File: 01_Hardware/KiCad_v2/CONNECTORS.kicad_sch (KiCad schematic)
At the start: 45 parts, among them J800 Conn_02x03_Odd_Even, J801 JST_B2B, J802 JST_B2B, J803 JST_B2B, J804 Conn_02x05_Odd_Even, J805 JST_B2B, J806 JST_B2B, J807 JST_B2B, J808 JST_B2B, SW800 SW_Push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

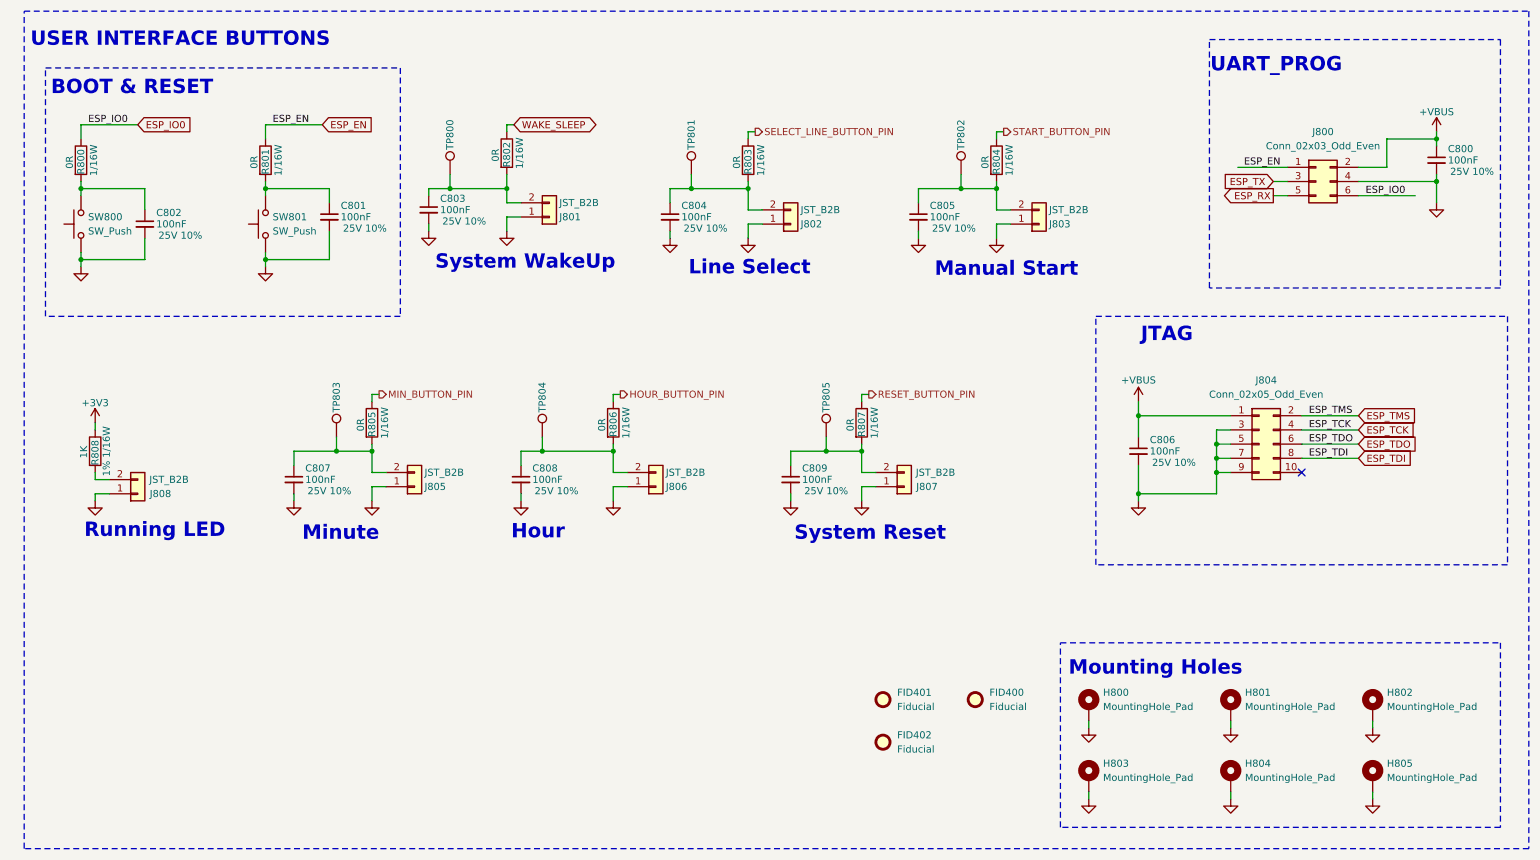
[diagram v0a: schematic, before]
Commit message: BOM done, except connectors/thermistor/button -> Will re-check BOM before sending to manufacturing
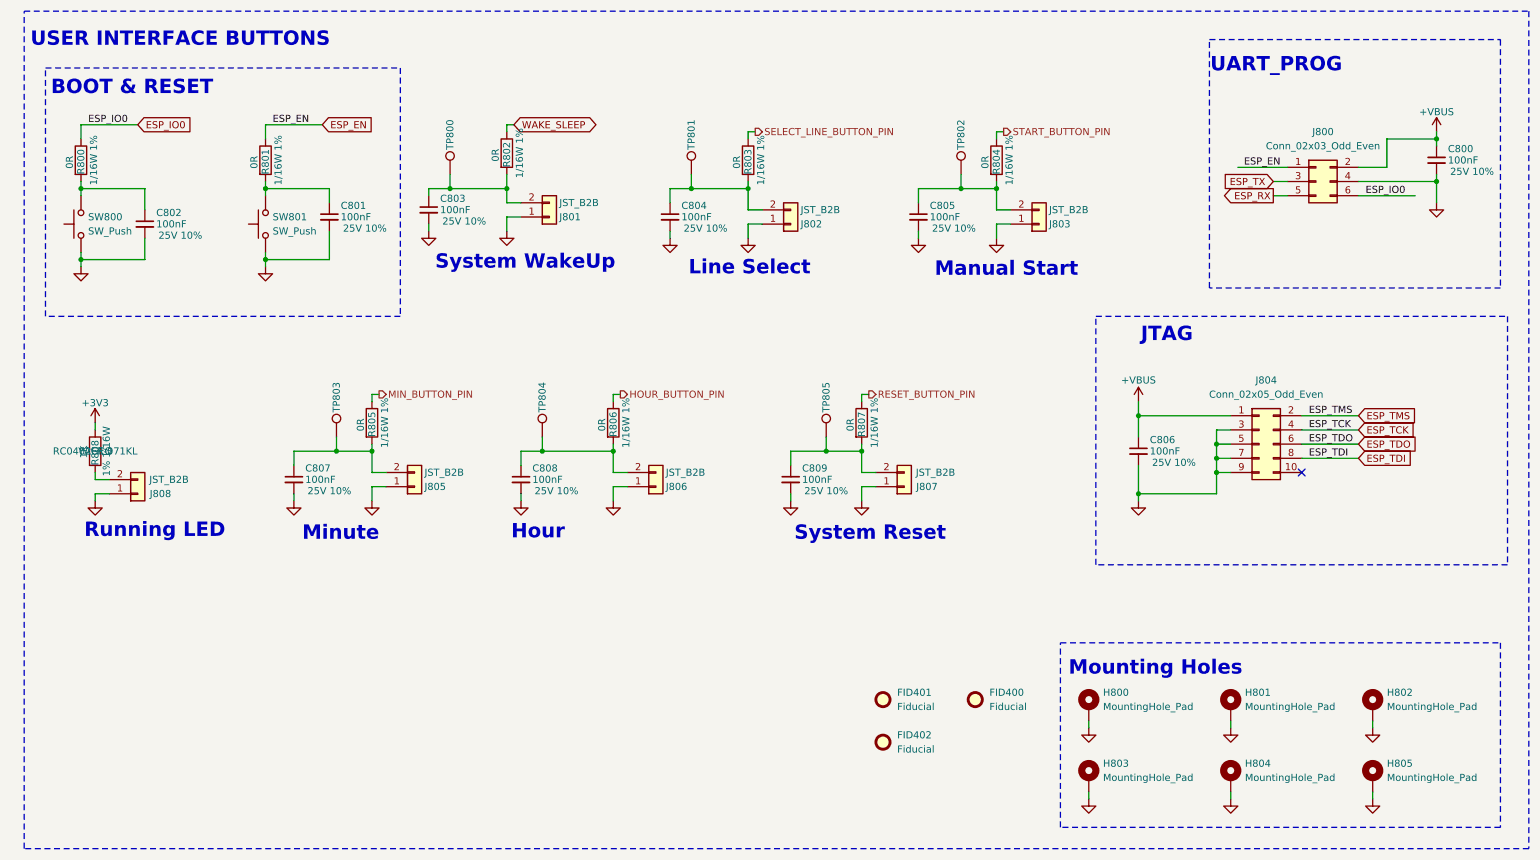
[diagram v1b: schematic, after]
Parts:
- C800, C801, C802, C803, C804, C805, C806, C807, C808, C809: Manufacturer Samsung Electro-Mechanics -> Samsung Electro-Mechanics
- R800, R801, R802, R803, R804, R805, R806, R807: Manufacturer (none) -> YAGEO; Manufacturer Part Number (none) -> AC0402FR-070RL
- R808: Manufacturer (none) -> YAGEO; Manufacturer Part Number (none) -> RC0402FR-071KL

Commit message: USB-C and Serial PCB routing done
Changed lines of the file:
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@@
 					(size 1.27 1.27)
 				)
+				(hide yes)
 			)
 		)
@@
 					(size 1.27 1.27)
 				)
+				(hide yes)
 			)
 		)
@@
 					(size 1.27 1.27)
 				)
+				(hide yes)
 			)
 		)
@@
 					(size 1.27 1.27)
 				)
+				(hide yes)
 			)
 		)

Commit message: Power plane/rearranged connectors
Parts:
- SW800, SW801: footprint Button_Switch_SMD:SW_SPST_PTS645 -> Custom_Global_Footprints:SW_101-C-W_XKB
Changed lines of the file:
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@@
 			)
 		)
-		(property "Footprint" "Button_Switch_SMD:SW_SPST_PTS645"
+		(property "Footprint" "Custom_Global_Footprints:SW_101-C-W_XKB"
 			(at 52.07 52.07 0)
 			(effects
@@
 			)
 		)
-		(property "Footprint" "Button_Switch_SMD:SW_SPST_PTS645"
+		(property "Footprint" "Custom_Global_Footprints:SW_101-C-W_XKB"
 			(at 19.05 52.07 0)
 			(effects

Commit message: Hardware for manufacturing v0.2
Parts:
- added TP400, TP401, TP404, TP406, TP407: TestPoint, TestPoint:TestPoint_Pad_1.5x1.5mm, symbol Connector:TestPoint
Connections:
- net GND: now also TP400.1, TP401.1, TP404.1, TP406.1, TP407.1
